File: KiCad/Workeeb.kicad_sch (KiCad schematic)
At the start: 100 parts

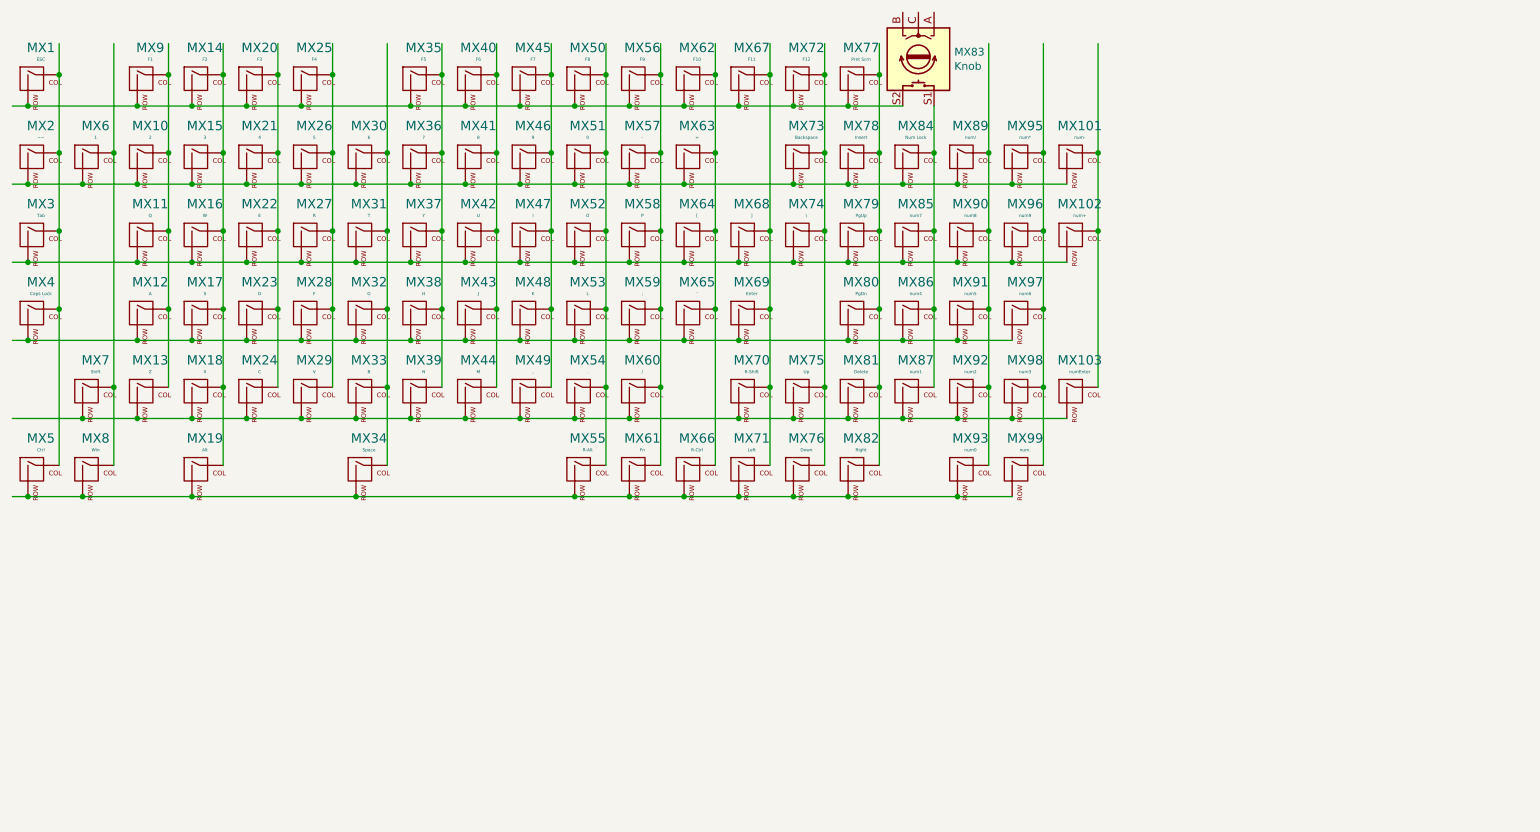
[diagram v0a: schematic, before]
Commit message: Finish duplex matrix for reducing pin count
Also add Keebio repos for Elite-C
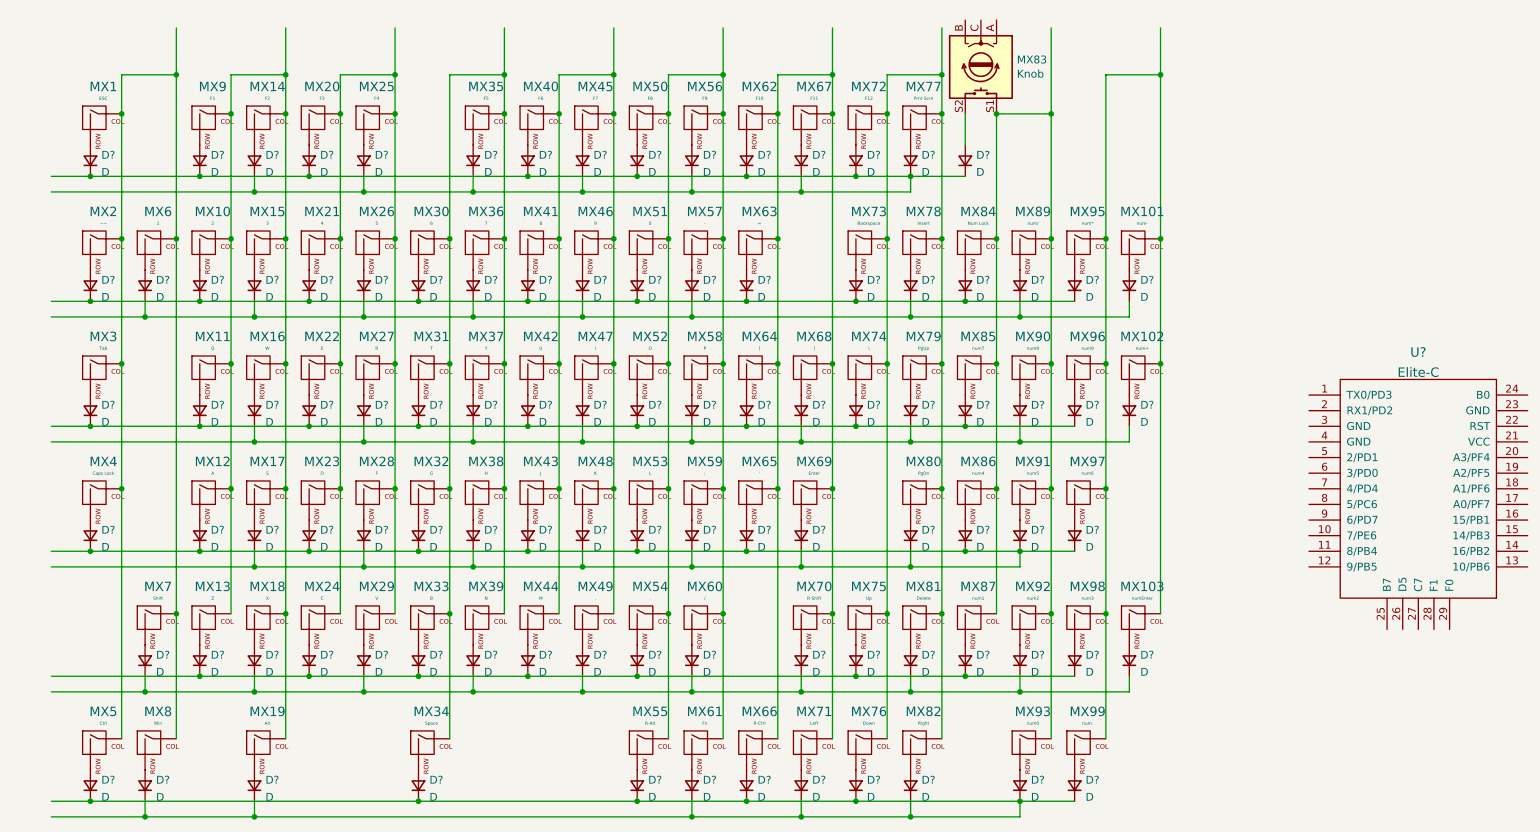
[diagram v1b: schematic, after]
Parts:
- added D? (x100): D, symbol Device:D_Small
- added U?: Elite-C, symbol keebio:Elite-C
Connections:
- net at MX1.1 (COL), MX2.1 (COL), MX3.1 (COL)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: now also MX6.1 (COL), MX7.1 (COL), MX8.1 (COL)
- net at MX14.1 (COL), MX15.1 (COL), MX16.1 (COL)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: now also MX10.1 (COL), MX11.1 (COL), MX12.1 (COL), MX13.1 (COL), MX9.1 (COL)
- net at MX25.1 (COL), MX26.1 (COL), MX27.1 (COL)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: now also MX20.1 (COL), MX21.1 (COL), MX22.1 (COL), MX23.1 (COL), MX24.1 (COL)
- net at MX35.1 (COL), MX36.1 (COL), MX37.1 (COL)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: now also MX30.1 (COL), MX31.1 (COL), MX32.1 (COL), MX33.1 (COL), MX34.1 (COL)
- net at MX40.1 (COL), MX41.1 (COL), MX42.1 (COL)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: now also MX45.1 (COL), MX46.1 (COL), MX47.1 (COL), MX48.1 (COL), MX49.1 (COL)
- net at MX50.1 (COL), MX51.1 (COL), MX52.1 (COL)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: now also MX56.1 (COL), MX57.1 (COL), MX58.1 (COL), MX59.1 (COL), MX60.1 (COL), MX61.1 (COL)
- net at MX62.1 (COL), MX63.1 (COL), MX64.1 (COL)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: now also MX67.1 (COL), MX68.1 (COL), MX69.1 (COL), MX70.1 (COL), MX71.1 (COL)
- net at MX72.1 (COL), MX73.1 (COL), MX74.1 (COL)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: now also MX77.1 (COL), MX78.1 (COL), MX79.1 (COL), MX80.1 (COL), MX81.1 (COL), MX82.1 (COL)
- net at MX83.S1, MX84.1 (COL), MX85.1 (COL)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: now also MX89.1 (COL), MX90.1 (COL), MX91.1 (COL), MX92.1 (COL), MX93.1 (COL)
- net at MX95.1 (COL), MX96.1 (COL), MX97.1 (COL)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: now also MX101.1 (COL), MX102.1 (COL), MX103.1 (COL)
- new net: D?.2 (A), MX2.2 (ROW)
- new net: D?.2 (A), MX6.2 (ROW)
- new net: D?.2 (A), MX15.2 (ROW)
- new net: D?.2 (A), MX10.2 (ROW)
- new net: D?.2 (A), MX26.2 (ROW)
- new net: D?.2 (A), MX21.2 (ROW)
- new net: D?.2 (A), MX36.2 (ROW)
- new net: D?.2 (A), MX30.2 (ROW)
- new net: D?.2 (A), MX41.2 (ROW)
- new net: D?.2 (A), MX51.2 (ROW)
- new net: D?.2 (A), MX46.2 (ROW)
- new net: D?.2 (A), MX63.2 (ROW)
- new net: D?.2 (A), MX57.2 (ROW)
- new net: D?.2 (A), MX72.2 (ROW)
- new net: D?.2 (A), MX67.2 (ROW)
- new net: D?.2 (A), MX73.2 (ROW)
- new net: D?.2 (A), MX11.2 (ROW)
- new net: D?.2 (A), MX3.2 (ROW)
- new net: D?.2 (A), MX22.2 (ROW)
- new net: D?.2 (A), MX16.2 (ROW)
- new net: D?.2 (A), MX31.2 (ROW)
- new net: D?.2 (A), MX27.2 (ROW)
- new net: D?.2 (A), MX42.2 (ROW)
- new net: D?.2 (A), MX37.2 (ROW)
- new net: D?.2 (A), MX47.2 (ROW)
- new net: D?.2 (A), MX58.2 (ROW)
- new net: D?.2 (A), MX52.2 (ROW)
- new net: D?.2 (A), MX68.2 (ROW)
- new net: D?.2 (A), MX64.2 (ROW)
- new net: D?.2 (A), MX74.2 (ROW)
- new net: D?.2 (A), MX4.2 (ROW)
- new net: D?.2 (A), MX32.2 (ROW)
- new net: D?.2 (A), MX43.2 (ROW)
- new net: D?.2 (A), MX38.2 (ROW)
- new net: D?.2 (A), MX48.2 (ROW)
- new net: D?.2 (A), MX59.2 (ROW)
- new net: D?.2 (A), MX53.2 (ROW)
- new net: D?.2 (A), MX69.2 (ROW)
- new net: D?.2 (A), MX65.2 (ROW)
- new net: D?.2 (A), MX28.2 (ROW)
- new net: D?.2 (A), MX17.2 (ROW)
- new net: D?.2 (A), MX23.2 (ROW)
- new net: D?.2 (A), MX12.2 (ROW)
- new net: D?.2 (A), MX33.2 (ROW)
- new net: D?.2 (A), MX44.2 (ROW)
- new net: D?.2 (A), MX39.2 (ROW)
- new net: D?.2 (A), MX49.2 (ROW)
- new net: D?.2 (A), MX60.2 (ROW)
- new net: D?.2 (A), MX54.2 (ROW)
- new net: D?.2 (A), MX70.2 (ROW)
- new net: D?.2 (A), MX29.2 (ROW)
- new net: D?.2 (A), MX18.2 (ROW)
- new net: D?.2 (A), MX24.2 (ROW)
- new net: D?.2 (A), MX13.2 (ROW)
- new net: D?.2 (A), MX7.2 (ROW)
- new net: D?.2 (A), MX75.2 (ROW)
- new net: D?.2 (A), MX5.2 (ROW)
- new net: D?.2 (A), MX8.2 (ROW)
- new net: D?.2 (A), MX19.2 (ROW)
- new net: D?.2 (A), MX34.2 (ROW)
- new net: D?.2 (A), MX55.2 (ROW)
- new net: D?.2 (A), MX61.2 (ROW)
- new net: D?.2 (A), MX66.2 (ROW)
- new net: D?.2 (A), MX76.2 (ROW)
- new net: D?.2 (A), MX71.2 (ROW)
- new net: D?.2 (A), MX62.2 (ROW)
- new net: D?.2 (A), MX56.2 (ROW)
- new net: D?.2 (A), MX50.2 (ROW)
- new net: D?.2 (A), MX45.2 (ROW)
- new net: D?.2 (A), MX40.2 (ROW)
- new net: D?.2 (A), MX35.2 (ROW)
- new net: D?.2 (A), MX25.2 (ROW)
- new net: D?.2 (A), MX20.2 (ROW)
- new net: D?.2 (A), MX14.2 (ROW)
- new net: D?.2 (A), MX9.2 (ROW)
- new net: D?.2 (A), MX1.2 (ROW)
- new net: D?.2 (A), MX77.2 (ROW)
- new net: D?.2 (A), MX78.2 (ROW)
- new net: D?.2 (A), MX79.2 (ROW)
- new net: D?.2 (A), MX80.2 (ROW)
- new net: D?.2 (A), MX81.2 (ROW)
- new net: D?.2 (A), MX82.2 (ROW)
- new net: D?.2 (A), MX84.2 (ROW)
- new net: D?.2 (A), MX85.2 (ROW)
- new net: D?.2 (A), MX86.2 (ROW)
- new net: D?.2 (A), MX87.2 (ROW)
- new net: D?.2 (A), MX89.2 (ROW)
- new net: D?.2 (A), MX90.2 (ROW)
- new net: D?.2 (A), MX91.2 (ROW)
- new net: D?.2 (A), MX92.2 (ROW)
- new net: D?.2 (A), MX93.2 (ROW)
- new net: D?.2 (A), MX95.2 (ROW)
- new net: D?.2 (A), MX96.2 (ROW)
- new net: D?.2 (A), MX97.2 (ROW)
- new net: D?.2 (A), MX98.2 (ROW)
- new net: D?.2 (A), MX99.2 (ROW)
- new net: D?.2 (A), MX101.2 (ROW)
- new net: D?.2 (A), MX102.2 (ROW)
- new net: D?.2 (A), MX103.2 (ROW)
- new net: D?.2 (A), MX83.S2
- new net: D?.1 (K), D?.1 (K), D?.1 (K), D?.1 (K), D?.1 (K), D?.1 (K), D?.1 (K), D?.1 (K), D?.1 (K), D?.1 (K) (x3)
- new net: D?.1 (K), D?.1 (K), D?.1 (K), D?.1 (K), D?.1 (K), D?.1 (K), D?.1 (K), D?.1 (K), D?.1 (K), D?.1 (K), D?.1 (K), D?.1 (K), D?.1 (K), D?.1 (K), D?.1 (K)
- new net: D?.1 (K), D?.1 (K), D?.1 (K), D?.1 (K), D?.1 (K), D?.1 (K), D?.1 (K), D?.1 (K)
- new net: D?.1 (K), D?.1 (K), D?.1 (K), D?.1 (K), D?.1 (K), D?.1 (K), D?.1 (K), D?.1 (K), D?.1 (K) (x2)
- new net: D?.1 (K), D?.1 (K), D?.1 (K), D?.1 (K), D?.1 (K), D?.1 (K), D?.1 (K), D?.1 (K), D?.1 (K), D?.1 (K), D?.1 (K), D?.1 (K)
- new net: D?.1 (K), D?.1 (K), D?.1 (K), D?.1 (K), D?.1 (K), D?.1 (K), D?.1 (K), D?.1 (K), D?.1 (K), D?.1 (K), D?.1 (K), D?.1 (K), D?.1 (K), D?.1 (K), D?.1 (K), D?.1 (K), D?.1 (K)
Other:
- moved on the sheet: MX1, MX10, MX101, MX102, MX103, MX11, MX12, MX13, MX14, MX15, MX16, MX17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

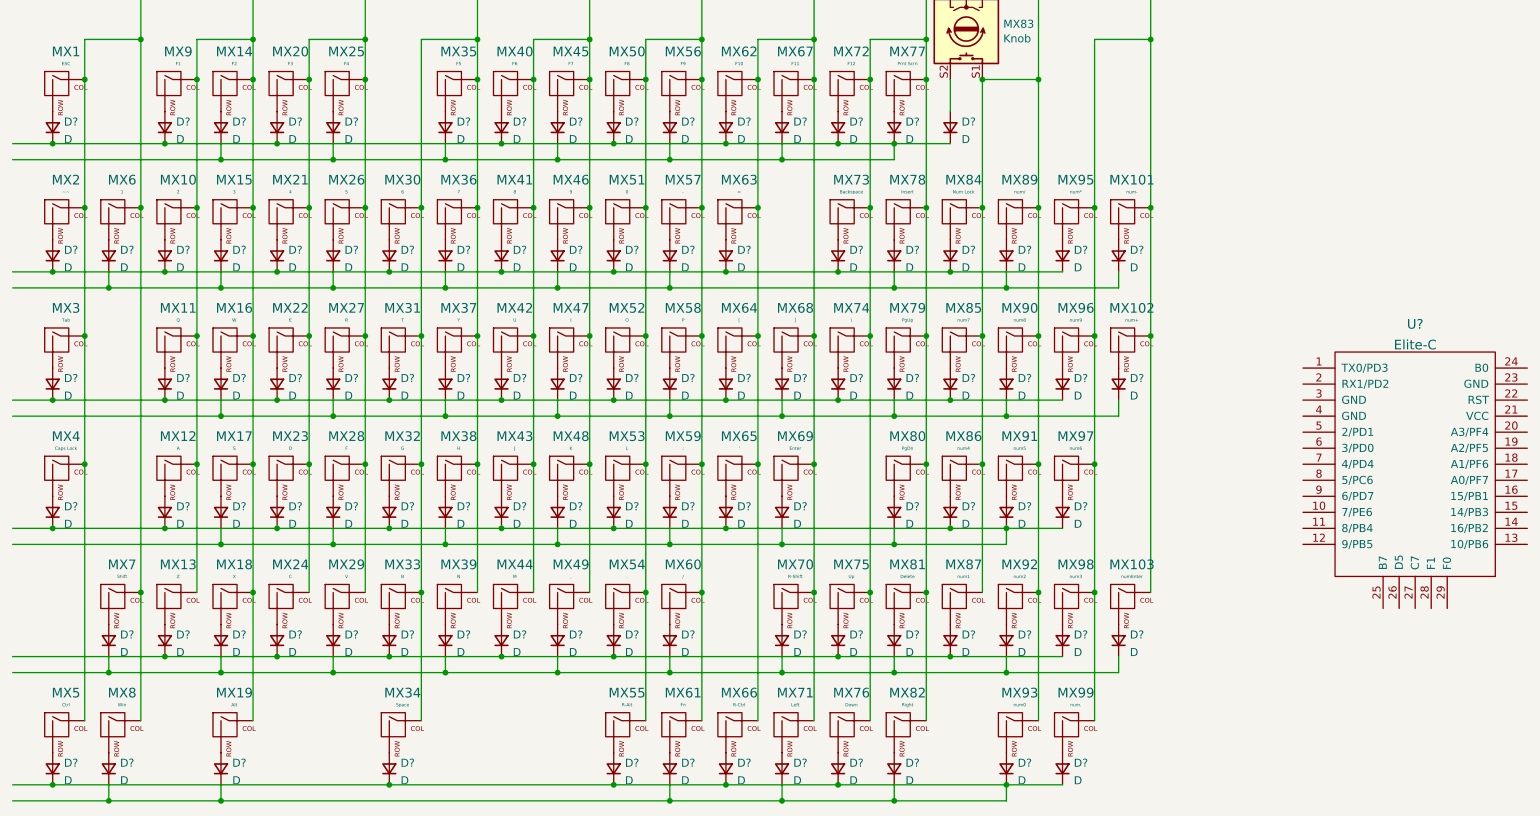
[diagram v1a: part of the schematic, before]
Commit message: Match up the diodes and Elite-C footprint
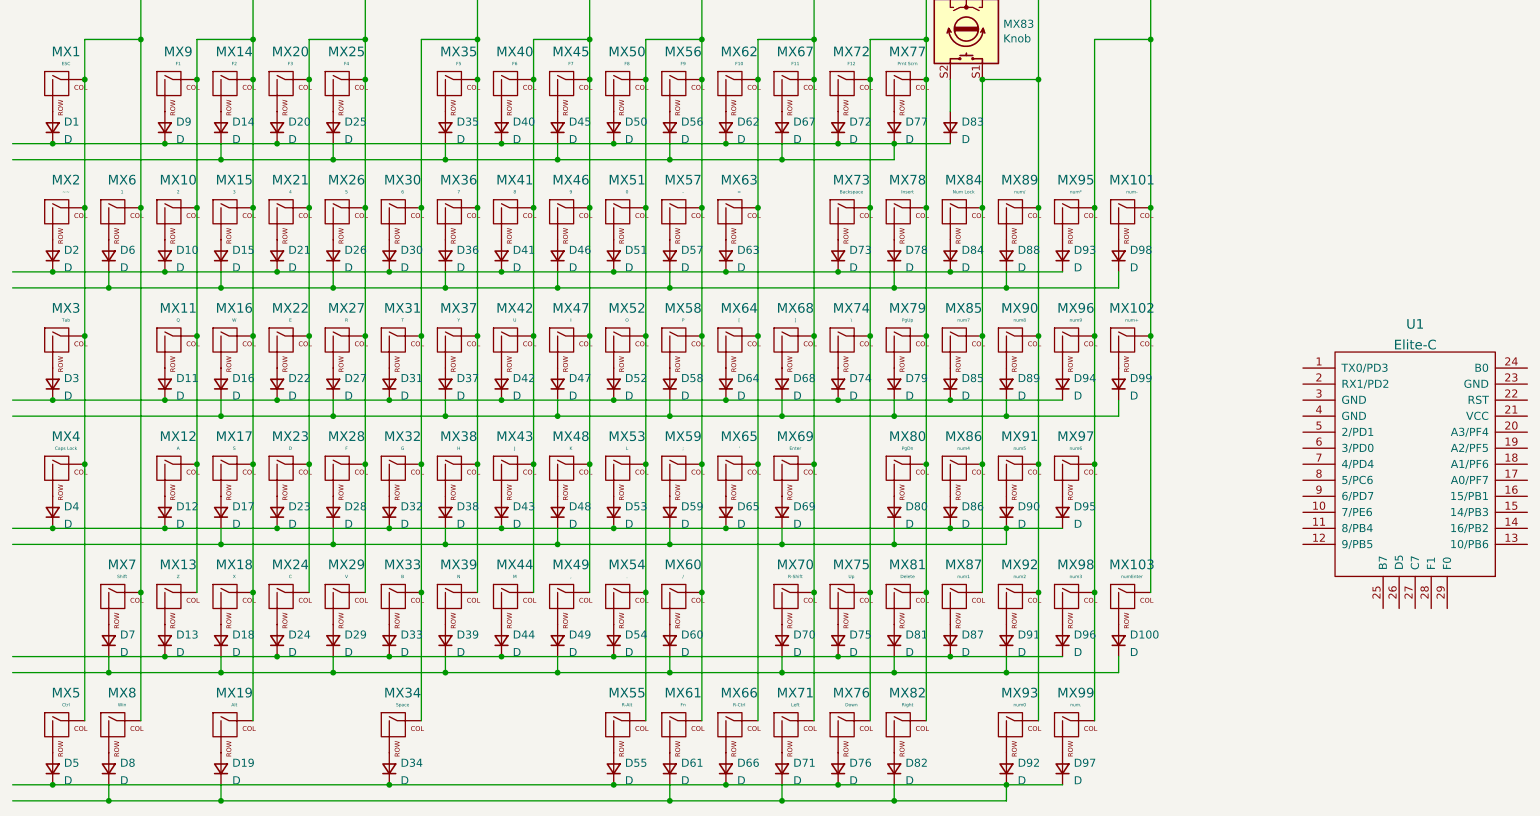
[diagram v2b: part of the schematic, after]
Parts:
- D1, D10, D100, D11, D12, D13, D14, D15, D16, D17, D18, D19, D2, D20, D21, D22, D23, D24, D25, D26, D27, D28, D29, D3, D30, D31, D32, D33, D34, D35, D36, D37, D38, D39, D4, D40, D41, D42, D43, D44, D45, D46, D47, D48, D49, D5, D50, D51, D52, D53, D54, D55, D56, D57, D58, D59, D6, D60, D61, D62, D63, D64, D65, D66, D67, D68, D69, D7, D70, D71, D72, D73, D74, D75, D76, D77, D78, D79, D8, D80, D81, D82, D83, D84, D85, D86, D87, D88, D89, D9, D90, D91, D92, D93, D94, D95, D96, D97, D98, D99: renamed from D?; footprint (none) -> Diode_SMD:D_SOD-123
- U1: renamed from U?; footprint (none) -> Keebio-Parts:Elite-C-castellated-29pin

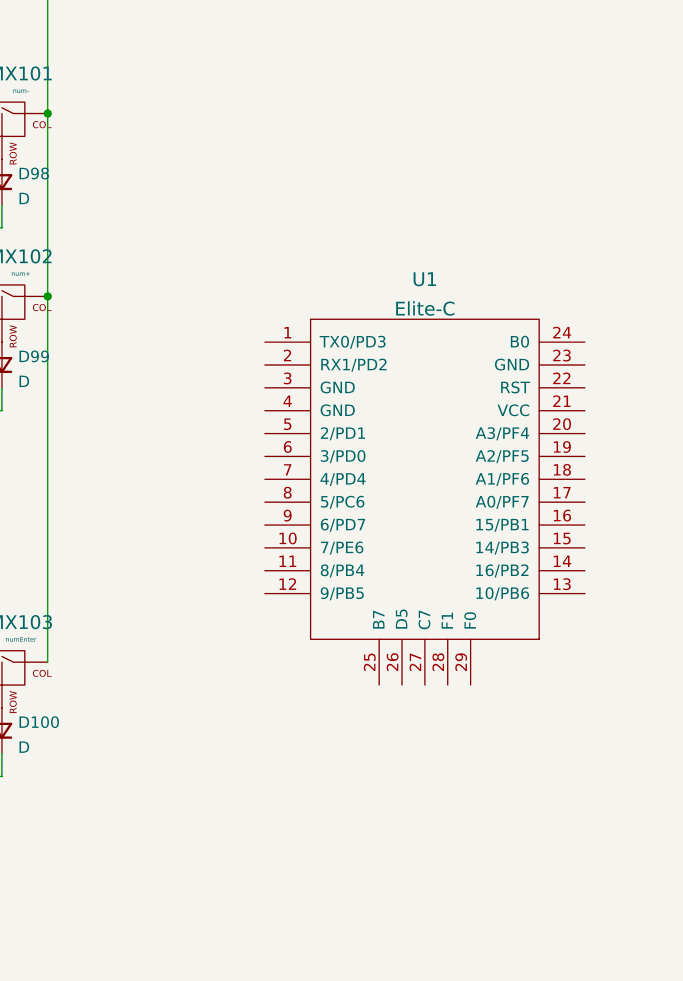
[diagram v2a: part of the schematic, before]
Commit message: Add EFM32HG322F64G-C-QFP48 symbol and footprint
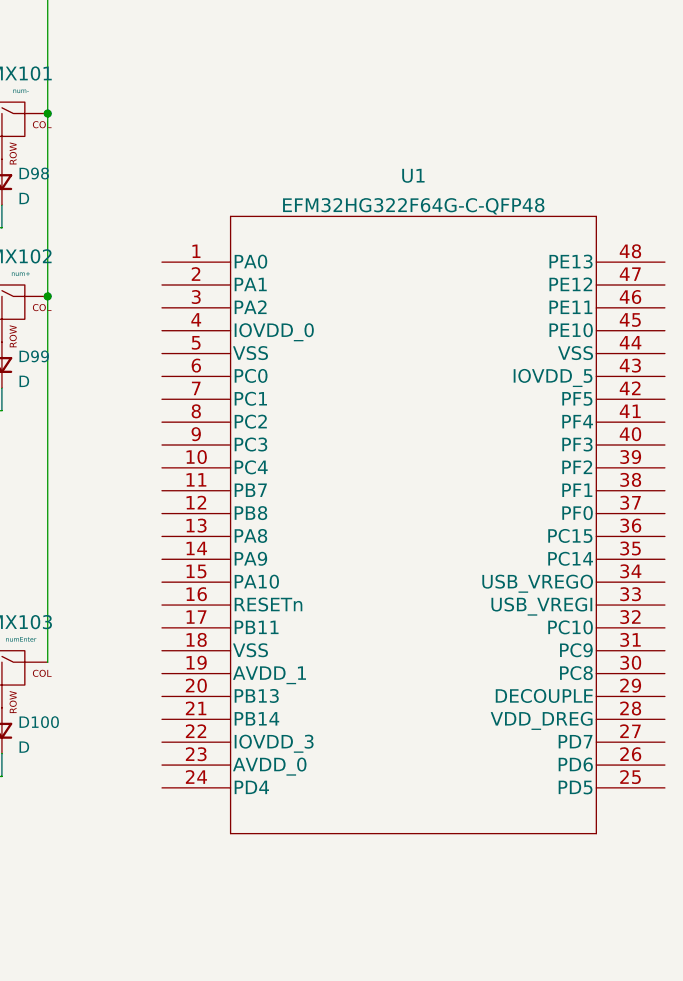
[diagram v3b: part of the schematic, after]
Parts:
- removed U1: Elite-C, Keebio-Parts:Elite-C-castellated-29pin, symbol keebio:Elite-C
- added U1: EFM32HG322F64G-C-QFP48, EFM32HG322F64G-C-QFP48:EFM32HG322F64G-C-QFP48, symbol EFM32HG322F64G-C-QFP48:EFM32HG322F64G-C-QFP48
